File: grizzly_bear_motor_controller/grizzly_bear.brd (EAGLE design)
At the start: 71 x 38.9 mm, 56 parts, among them Q1 PH7030L, Q2 PH7030L, Q3 PH7030L, Q4 PH7030L, Q5 FDD4141TO252, U1 A4940, U2 ATMEGA32U4-AU, U3 ACS714, U4 UA78L00, Y1 16MHz

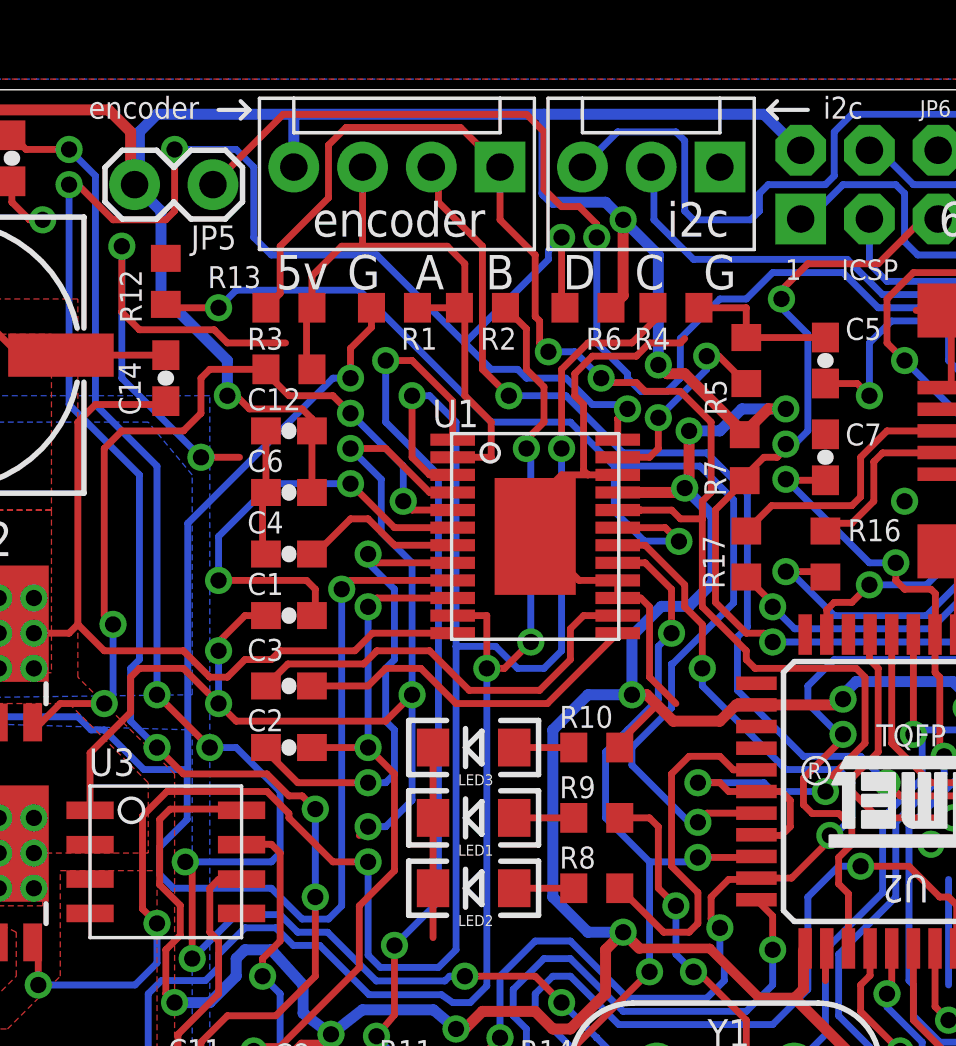
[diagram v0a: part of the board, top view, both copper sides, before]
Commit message: Fix mistake with AHI shorted to ENC2
Change-Id: I23787c04aa77e54cc0262fec6cb01ab894f515dc
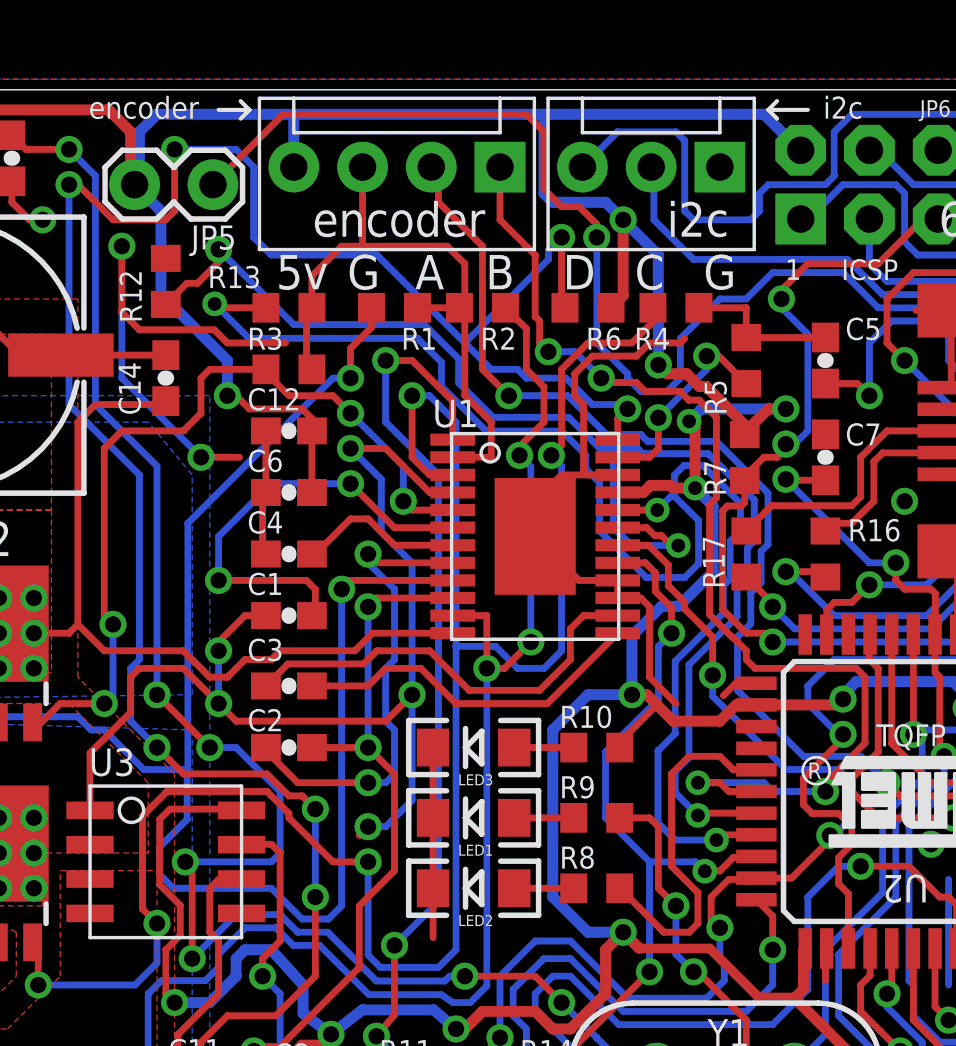
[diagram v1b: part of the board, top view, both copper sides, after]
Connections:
- new net AHI: R13.1, U1.20, U2.30
- net ENC2: no longer R13.1, U1.20, U2.30
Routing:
- net AHI: track 0.00 -> 52.3 mm, vias 0 -> 3
- net ENC2: track 62.6 -> 41.6 mm
- net N$22: track 48.5 -> 50.9 mm
- net GND: track 133.5 -> 134.8 mm
- net ENC1: track 42.5 -> 43.6 mm

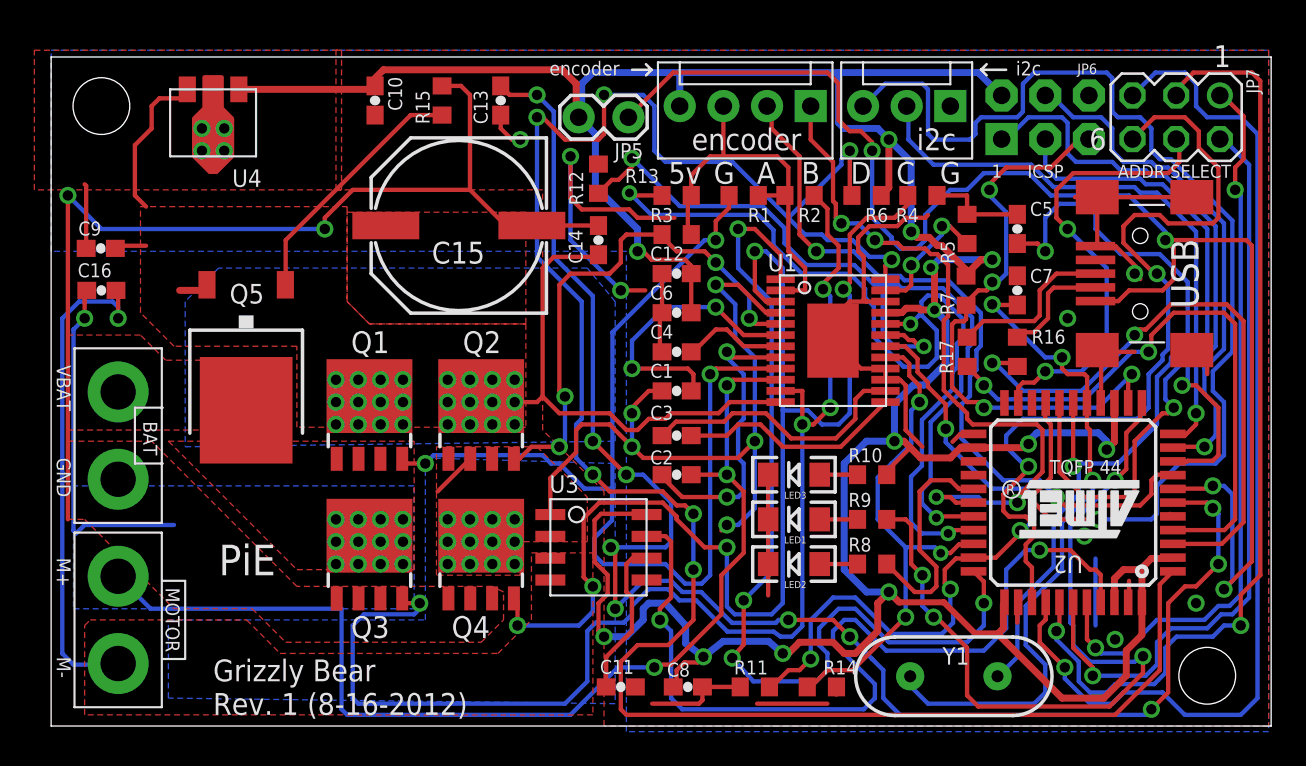
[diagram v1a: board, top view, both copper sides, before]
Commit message: Fix 18pF caps and renumber all passives
Change-Id: Id4e7dc3682557a51dcb971b0b6fbe1525da739df
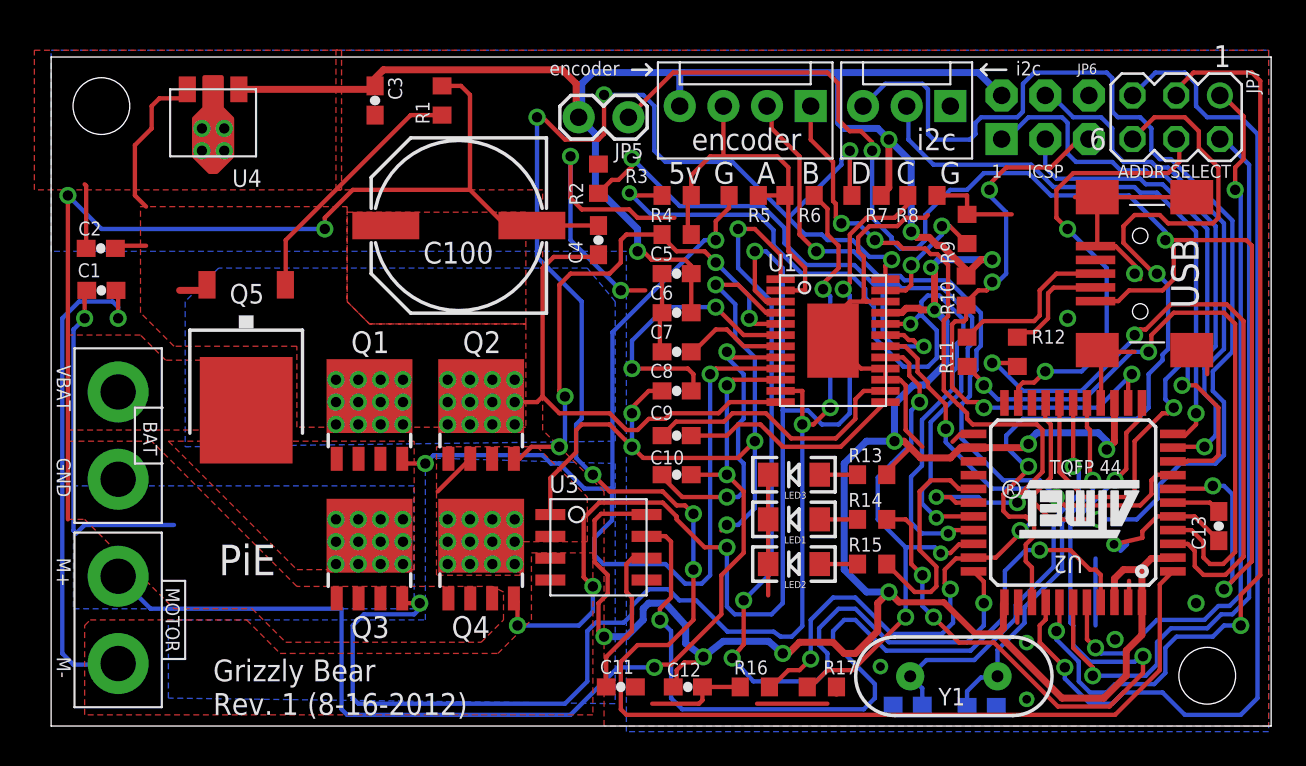
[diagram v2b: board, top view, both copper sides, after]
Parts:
- removed C16: 0.1uF, SparkFun-Passives:0603-CAP
- added C100: 470uF, SparkFun-Passives:PANASONIC_G
- C1: value 36nF -> 0.1uF
- C10, C8: value 0.1uF -> 36nF
- C14: value 10uF -> 18pF
- C15: value 470uF -> 18pF; device SparkFun-Passives:PANASONIC_G -> SparkFun-Passives:0603-CAP
- C2: value 36nF -> 0.33uF
- C3: value 470nF -> 0.1uF
- C4: value 1uF -> 10uF
- C5: value 18pF -> 0.1uF
- C7: value 18pF -> 1uF
- C9: value 0.33uF -> 470nF
- R10: value 330 -> 10k; device resistor:R0603 -> rcl:R0603
- R11, R12: value 10k -> 22; device resistor:R0603 -> rcl:R0603
- R13, R14, R15: value 10k -> 330
- R16, R17: value 22 -> 10k; device rcl:R0603 -> resistor:R0603
- R5: value 47k -> 10k
- R7: device rcl:R0603 -> resistor:R0603
- R8: value 330 -> 10k
- R9: value 330 -> 47k
- moved C13 48.6 mm to (67.9, 10.3)
- moved C15 41.3 mm to (54.1, -0.16), flipped to the bottom, turned to 0 degrees
- moved R15 36.8 mm to (47.8, 8.12), turned to 180 degrees
- moved C2 36.0 mm to (2.89, 26.5), turned to 180 degrees
- moved C9 35.2 mm to (36.4, 15.6), turned to 0 degrees
- moved C1 34.0 mm to (2.92, 24.1)
- moved C14 32.5 mm to (49.8, -0.09), flipped to the bottom, turned to 180 degrees
- moved C10 28.0 mm to (36.4, 13.3), turned to 0 degrees
- moved R12 26.4 mm to (56.2, 20.5), turned to 270 degrees
- moved C3 26.2 mm to (18.9, 35.1), turned to 270 degrees
- moved R16 24.8 mm to (41.0, 0.97), turned to 180 degrees
- moved C12 24.1 mm to (37.0, 0.97)
- moved R11 23.1 mm to (53.3, 20.5), turned to 270 degrees
- moved R8 21.6 mm to (50.7, 29.6), turned to 0 degrees
- moved R17 21.3 mm to (44.9, 0.97), turned to 0 degrees
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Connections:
- net 5V: now also C12.1, C3.1, C5.2, R10.1, R13.2, R7.2; no longer C10.1, C12.2, C8.1, R10.2, R6.2, R7.1
- net AHI: now also R3.1; no longer R13.1
- net BATGND: now also C100.-, C4.1, R1.1; no longer C14.1, C15.-, R15.1
- net FAULT: now also R7.1; no longer R6.1
- net GND: now also C12.2, C14.1, C15.1, C2.2, C3.2, C7.2, R16.2, R17.2, R6.2, R8.2, R9.2; no longer C10.2, C12.1, C4.2, C7.1, C8.2, C9.2, R1.2, R11.2, R12.2, R13.2, R14.2
- net GREEN: now also R15.1; no longer R8.1
- net M+: now also C1.1, C10.2; no longer C16.1, C2.2
- net M-(POST): now also C1.2; no longer C16.2
- net N$1: now also R1.2; no longer R15.2
- net N$11: now also R8.1; no longer R4.1
- net N$13: now also R4.1; no longer R3.1
- net N$14: now also C8.2; no longer C1.2
- net N$16: now also C10.1; no longer C2.1
- net N$17: now also C7.1; no longer C4.1
- net N$19: now also C9.1; no longer C3.1
- net N$2: now also R5.1; no longer R1.1
- net N$20: now also R17.1; no longer R14.1
- net N$21: now also R16.1; no longer R11.1
- net N$22: now also R2.1; no longer R12.1
- net N$23: now also R14.2; no longer R9.2
- net N$24: now also R11.1; no longer R17.1
- net N$25: now also R13.1; no longer R10.1
- net N$26: now also C14.2; no longer C5.2
- net N$27: now also C15.2; no longer C7.2
- net N$29: now also R12.1; no longer R16.1
- net N$3: now also C9.2; no longer C3.2
- net N$5: now also R15.2; no longer R8.2
- net N$6: now also R9.1; no longer R5.1
- net N$7: now also R12.2; no longer R16.2
- net N$8: now also R6.1; no longer R2.1
- net N$9: now also R11.2; no longer R17.2
- net RED: now also R14.1; no longer R9.1
- net RESET: now also R10.2; no longer R7.2
- net SGH: now also C8.1; no longer C1.1
- net VBAT: now also C100.+, C2.1, C4.2; no longer C14.2, C15.+, C9.1
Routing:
- net N$18: track 92.4 -> 2.88 mm, vias 10 -> 0
- net N$26: track 47.9 -> 23.7 mm, vias 2 -> 1
- net N$27: track 38.8 -> 21.7 mm, vias 3 -> 1
- net GND: track 134.8 -> 140.8 mm, vias 12 -> 14
- net N$9: track 34.7 -> 38.0 mm
- net N$7: track 35.8 -> 39.0 mm
- net RED: track 46.1 -> 44.5 mm
- net SDA: track 68.0 -> 67.5 mm

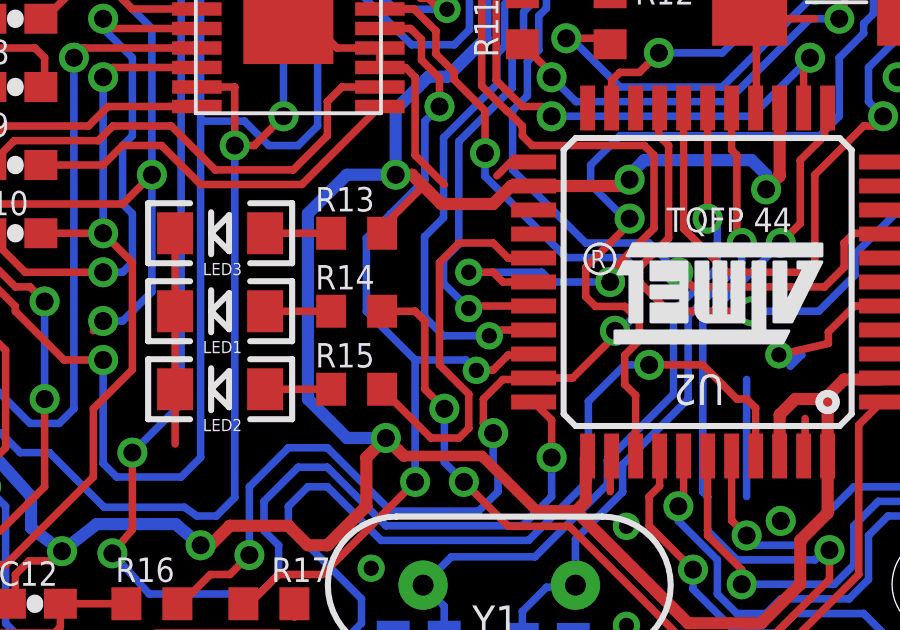
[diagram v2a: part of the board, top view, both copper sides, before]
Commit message: Swap PWM pins on one side of bridge to allow locked-antiphase PWM.
Change-Id: I960fdec47b52c005c589c20b71f3d1438955e5d5
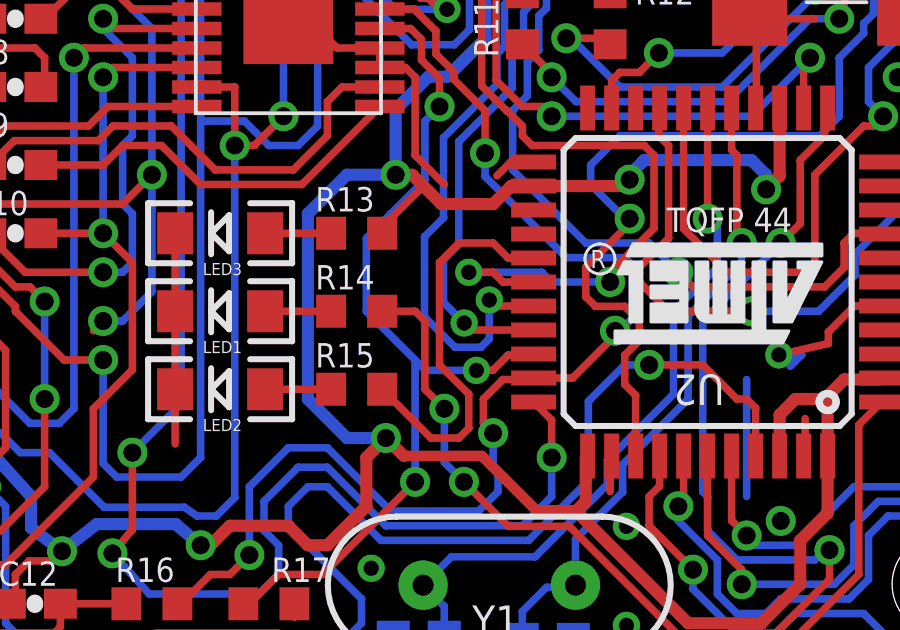
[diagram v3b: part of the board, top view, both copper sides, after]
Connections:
- net AHI: now also U2.29; no longer U2.30
- net N$22: now also U2.30; no longer U2.29
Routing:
- net AHI: track 52.3 -> 53.8 mm
- net N$22: track 50.9 -> 51.6 mm
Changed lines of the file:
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@@
 <setting verticaltext="up"/>
 </settings>
-<grid distance="0.05" unitdist="inch" unit="inch" style="dots" multiple="1" display="yes" altdistance="0.005" altunitdist="inch" altunit="inch"/>
+<grid distance="0.05" unitdist="inch" unit="inch" style="dots" multiple="1" display="yes" altdistance="0.001" altunitdist="inch" altunit="inch"/>
 <layers>
 <layer number="1" name="Top" color="4" fill="1" visible="yes" active="yes"/>
@@
 <layer number="23" name="tOrigins" color="15" fill="1" visible="yes" active="yes"/>
 <layer number="24" name="bOrigins" color="15" fill="1" visible="yes" active="yes"/>
-<layer number="25" name="tNames" color="7" fill="1" visible="yes" active="yes"/>
-<layer number="26" name="bNames" color="12" fill="1" visible="yes" active="yes"/>
-<layer number="27" name="tValues" color="7" fill="1" visible="yes" active="yes"/>
-<layer number="28" name="bValues" color="12" fill="1" visible="yes" active="yes"/>
+<layer number="25" name="tNames" color="7" fill="1" visible="no" active="yes"/>
+<layer number="26" name="bNames" color="12" fill="1" visible="no" active="yes"/>
+<layer number="27" name="tValues" color="7" fill="1" visible="no" active="yes"/>
+<layer number="28" name="bValues" color="12" fill="1" visible="no" active="yes"/>
 <layer number="29" name="tStop" color="7" fill="3" visible="no" active="yes"/>
 <layer number="30" name="bStop" color="7" fill="6" visible="no" active="yes"/>
@@
 <wire x1="48.9125" y1="13.975" x2="48.1" y2="13.1625" width="0.254" layer="16"/>
 <wire x1="48.1" y1="13.1625" x2="48.1" y2="10.725003125" width="0.254" layer="16"/>
-<wire x1="48.1" y1="10.725003125" x2="49.725003125" y2="9.1" width="0.254" layer="16"/>
+<wire x1="48.1" y1="10.725003125" x2="49.097503125" y2="9.7275" width="0.254" layer="16"/>
+<wire x1="49.097503125" y1="9.7275" x2="49.725003125" y2="9.1" width="0.254" layer="16"/>
 <wire x1="48.55" y1="20.15" x2="49.573" y2="20.15" width="0.254" layer="1"/>
 <wire x1="49.573" y1="20.15" x2="49.9364" y2="19.7866" width="0.254" layer="1"/>
@@
 <wire x1="52.324" y1="8.763" x2="51.775003125" y2="8.763" width="0.254" layer="1"/>
 <wire x1="51.775003125" y1="8.763" x2="51.766503125" y2="8.7545" width="0.254" layer="1"/>
-<wire x1="49.725003125" y1="9.1" x2="51.421003125" y2="9.1" width="0.254" layer="16"/>
-<wire x1="51.421003125" y1="9.1" x2="51.766503125" y2="8.7545" width="0.254" layer="16"/>
+<wire x1="51.766503125" y1="8.7545" x2="50.070503125" y2="8.7545" width="0.254" layer="16"/>
+<wire x1="50.070503125" y1="8.7545" x2="49.725003125" y2="9.1" width="0.254" layer="16"/>
 </signal>
 <signal name="N$21">
@@
 <contactref element="U1" pad="19"/>
 <contactref element="R2" pad="1"/>
-<contactref element="U2" pad="29"/>
 <wire x1="31.85" y1="29.7" x2="31.975" y2="29.575" width="0.254" layer="1"/>
 <via x="33.8" y="31.734" extent="1-16" drill="0.6"/>
 <via x="50.786603125" y="20.7896" extent="1-16" drill="0.508"/>
-<via x="51.512503125" y="10.8165" extent="1-16" drill="0.508"/>
+<via x="51.360103125" y="10.3339" extent="1-16" drill="0.508"/>
 <wire x1="50.786603125" y1="20.7896" x2="49.0604" y2="20.7896" width="0.254" layer="16"/>
 <wire x1="46.736" y1="25.527" x2="43.942" y2="25.527" width="0.254" layer="16"/>
@@
 <wire x1="51.181" y1="16.383" x2="51.181" y2="12.954" width="0.254" layer="16"/>
 <wire x1="50.673" y1="12.446" x2="51.181" y2="12.954" width="0.254" layer="16"/>
-<wire x1="53.67500625" y1="10.9" x2="51.596003125" y2="10.9" width="0.254" layer="1"/>
-<wire x1="51.596003125" y1="10.9" x2="51.512503125" y2="10.8165" width="0.254" layer="1"/>
-<wire x1="50.673" y1="12.446" x2="50.673" y2="11.656003125" width="0.254" layer="16"/>
-<wire x1="50.673" y1="11.656003125" x2="51.512503125" y2="10.8165" width="0.254" layer="16"/>
+<wire x1="50.673" y1="12.446" x2="50.673" y2="11.021003125" width="0.254" layer="16"/>
 <wire x1="51.181" y1="16.383" x2="52.959" y2="18.161" width="0.254" layer="16"/>
+<contactref element="U2" pad="30"/>
+<wire x1="50.673" y1="11.021003125" x2="51.360103125" y2="10.3339" width="0.254" layer="16"/>
+<wire x1="53.67500625" y1="10.1" x2="51.594003125" y2="10.1" width="0.254" layer="1"/>
+<wire x1="51.594003125" y1="10.1" x2="51.360103125" y2="10.3339" width="0.254" layer="1"/>
 </signal>
 <signal name="5V">
@@
 <contactref element="U1" pad="20"/>
 <contactref element="R3" pad="1"/>
-<contactref element="U2" pad="30"/>
 <wire x1="51.5366" y1="21.717" x2="51.5366" y2="20.1168" width="0.254" layer="16"/>
 <wire x1="51.5366" y1="20.1168" x2="51.0286" y2="19.6088" width="0.254" layer="16"/>
@@
 <wire x1="51.0032" y1="23.749" x2="51.689" y2="23.749" width="0.254" layer="16"/>
 <wire x1="51.689" y1="23.749" x2="53.086" y2="22.352" width="0.254" layer="16"/>
-<via x="52.197" y="9.906" extent="1-16" drill="0.508"/>
+<via x="52.197" y="11.0998" extent="1-16" drill="0.508"/>
 <wire x1="50.038" y1="10.541" x2="50.038" y2="13.208" width="0.254" layer="16"/>
 <wire x1="50.038" y1="13.208" x2="50.673" y2="13.843" width="0.254" layer="16"/>
-<wire x1="53.67500625" y1="10.1" x2="52.391" y2="10.1" width="0.254" layer="1"/>
-<wire x1="52.391" y1="10.1" x2="52.197" y2="9.906" width="0.254" layer="1"/>
-<wire x1="52.197" y1="9.906" x2="50.673" y2="9.906" width="0.254" layer="16"/>
-<wire x1="50.673" y1="9.906" x2="50.038" y2="10.541" width="0.254" layer="16"/>
+<wire x1="51.054" y1="9.525" x2="50.038" y2="10.541" width="0.254" layer="16"/>
 <wire x1="50.673" y1="16.51" x2="52.451" y2="18.288" width="0.254" layer="16"/>
+<contactref element="U2" pad="29"/>
+<wire x1="51.054" y1="9.525" x2="51.9176" y2="9.525" width="0.254" layer="16"/>
+<wire x1="52.197" y1="11.0998" x2="52.197" y2="9.8044" width="0.254" layer="16"/>
+<wire x1="52.197" y1="9.8044" x2="51.9176" y2="9.525" width="0.254" layer="16"/>
+<wire x1="53.67500625" y1="10.9" x2="52.3968" y2="10.9" width="0.254" layer="1"/>
+<wire x1="52.3968" y1="10.9" x2="52.197" y2="11.0998" width="0.254" layer="1"/>
 </signal>
 </signals>
